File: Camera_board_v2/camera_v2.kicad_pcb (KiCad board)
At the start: 2 copper layers, 21.4 x 36.6 mm, 30 parts, among them J1 Conn_01x01, J2 Conn_01x05, J7 FC Connector, J8 I2C1 Breakout, Q1 BSS83P, Q2 BSS138, U2 TLV74315, U3 TLV74328, X1 CAMERA_OV2640

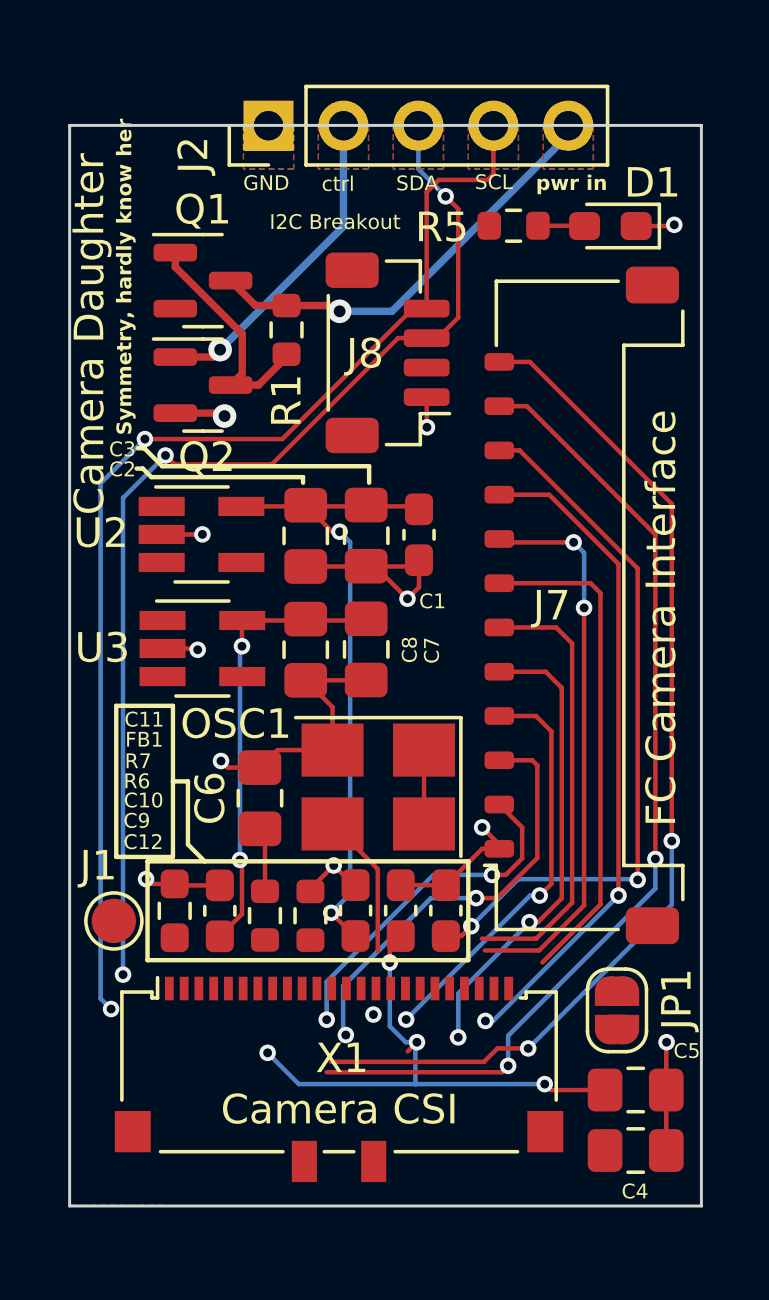
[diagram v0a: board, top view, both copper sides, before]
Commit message: finished?
everything is connected, but theres a few errors - idk how significant those are
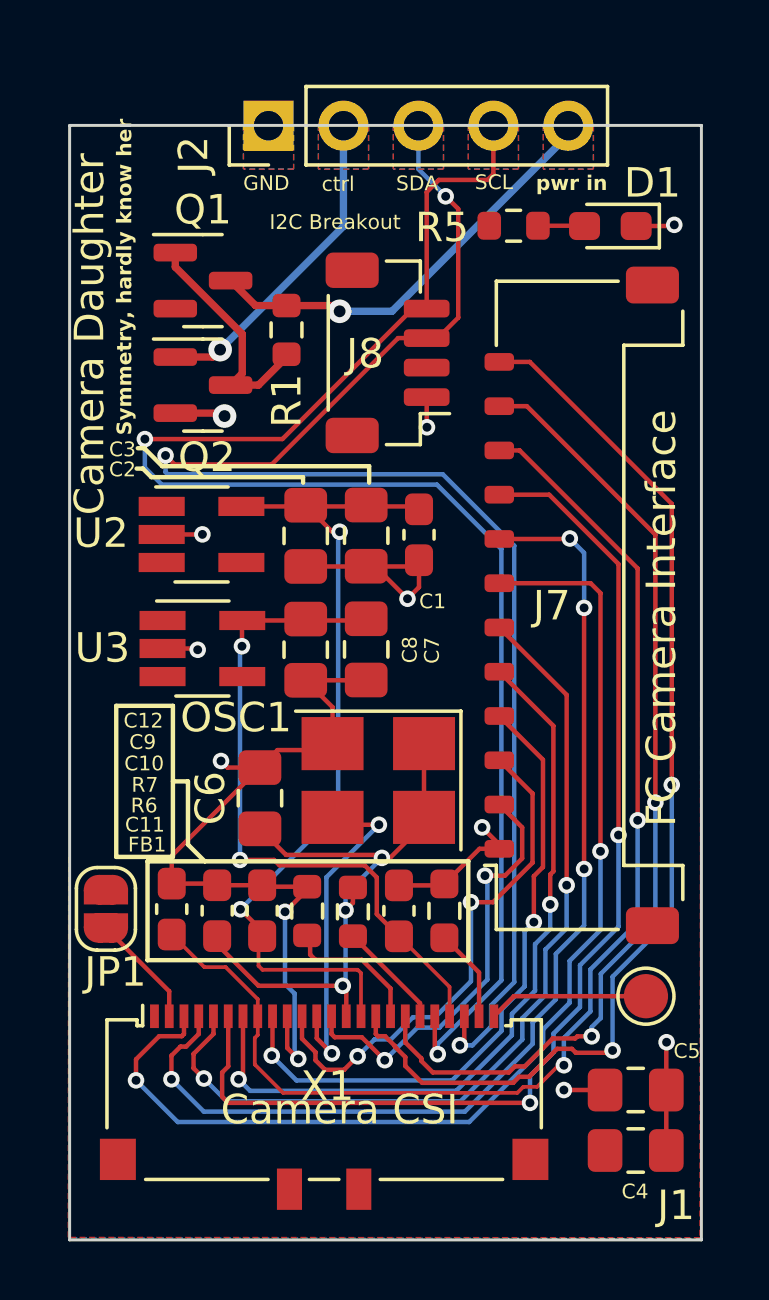
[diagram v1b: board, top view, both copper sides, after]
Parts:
- removed G***: LOGO, LOGO
- moved J1 18.2 mm to (166.5, 135.2)
- moved JP1 17.7 mm to (148.2, 132.2)
- moved C12 9.29 mm to (150.4, 132.2)
- moved FB1 9.14 mm to (159.7, 132.3)
- moved C9 6.22 mm to (151.9, 132.3)
- moved C11 6.07 mm to (158.1, 132.3)
- moved C10 3.17 mm to (153.5, 132.3)
- moved R6 2.98 mm to (156.6, 132.3)
- moved X1 1.07 mm to (155.6, 138.9)
- moved OSC1 0.22 mm to (157.4, 127.8)
- moved R7 0.19 mm to (155.0, 132.3)
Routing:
- net D4: track 16.9 -> 38.5 mm, vias 0 -> 2
- net ENAB_RF / D3: track 19.0 -> 36.7 mm, vias 2 -> 4
- net VBUS_RESET / PC: track 24.2 -> 41.6 mm
- net I2C_RESET / D2: track 22.5 -> 37.8 mm
- net D5: track 15.0 -> 30.0 mm, vias 0 -> 2
- net SDA1: track 37.2 -> 51.4 mm
- net SCL1: track 39.4 -> 52.8 mm
- net GND: track 36.1 -> 49.3 mm
- net D6: track 16.0 -> 26.1 mm
- net ENABLE_BURN / D7: track 14.0 -> 22.0 mm
- net 2.8V: track 15.6 -> 23.3 mm
- net 1.5V: track 22.2 -> 29.1 mm, vias 3 -> 2
- net Net-(OSC1-OUT): track 4.95 -> 11.6 mm, vias 0 -> 2
- net Net-(J1-Pin_1): track 0.00 -> 5.44 mm
- net Net-(X1-PWDN): track 0.24 -> 4.83 mm
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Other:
- board size 21.4 x 36.6 mm -> 21.4 x 37.8 mm

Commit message: might be too big
added meme to the back - board might be too long
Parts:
- added G***: LOGO, LOGO, B.Cu at (156.6, 121.0)
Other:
- board text added: "What do you mean I have to flip the whole board?"

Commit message: small fixes
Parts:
- moved JP1 0.25 mm to (148.4, 132.3)
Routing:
- net +3V3: track 22.6 -> 33.6 mm, vias 4 -> 6

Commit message: Updated Camera Board V2 with Production Files
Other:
- board text added: "Camera Daughter Board V2 By Nicole Maggard Updated By Kelly Williams C.2024"
- board text removed: "Camera Daughter Board V1 By Nicole Maggard"
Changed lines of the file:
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@@
 			)
 		)
-		(property "Footprint" ""
+		(property "Footprint" "Capacitor_SMD:C_0805_2012Metric_Pad1.18x1.45mm_HandSolder"
 			(at 0 0 -90)
 			(unlocked yes)
@@
 			)
 		)
-		(property "Footprint" ""
+		(property "Footprint" "Oscillator:Oscillator_SMD_SeikoEpson_SG8002CE-4Pin_3.2x2.5mm_HandSoldering"
 			(at 0 0 180)
 			(unlocked yes)
@@
 			)
 		)
-		(property "Footprint" ""
+		(property "Footprint" "Jumper:SolderJumper-2_P1.3mm_Open_RoundedPad1.0x1.5mm"
 			(at 0 0 90)
 			(unlocked yes)
@@
 			)
 		)
-		(property "Footprint" ""
+		(property "Footprint" "Capacitor_SMD:C_0603_1608Metric_Pad1.08x0.95mm_HandSolder"
 			(at 0 0 -90)
 			(unlocked yes)
@@
 			)
 		)
-		(property "Footprint" ""
+		(property "Footprint" "Capacitor_SMD:C_0805_2012Metric_Pad1.18x1.45mm_HandSolder"
 			(at 0 0 90)
 			(unlocked yes)
@@
 			)
 		)
-		(property "Footprint" ""
+		(property "Footprint" "Capacitor_SMD:C_0603_1608Metric_Pad1.08x0.95mm_HandSolder"
 			(at 0 0 90)
 			(unlocked yes)
@@
 			)
 		)
-		(property "Footprint" ""
+		(property "Footprint" "Capacitor_SMD:C_0805_2012Metric_Pad1.18x1.45mm_HandSolder"
 			(at 0 0 0)
 			(unlocked yes)
@@
 			)
 		)
-		(property "Footprint" ""
+		(property "Footprint" "Connector_Molex:Molex_Pico-Lock_504050-1291_1x12-1MP_P1.50mm_Horizontal"
 			(at 0 0 90)
 			(unlocked yes)
@@
 			)
 		)
-		(property "Footprint" ""
+		(property "Footprint" "Resistor_SMD:R_0603_1608Metric"
 			(at 0 0 90)
 			(unlocked yes)
@@
 			)
 		)
-		(property "Footprint" ""
+		(property "Footprint" "Package_TO_SOT_SMD:SOT-23-5_HandSoldering"
 			(at 0 0 0)
 			(unlocked yes)
@@
 			)
 		)
-		(property "Footprint" ""
+		(property "Footprint" "Capacitor_SMD:C_0603_1608Metric_Pad1.08x0.95mm_HandSolder"
 			(at 0 0 90)
 			(unlocked yes)
@@
 			)
 		)
-		(property "Footprint" ""
+		(property "Footprint" "Package_TO_SOT_SMD:SOT-23-5_HandSoldering"
 			(at 0 0 0)
 			(unlocked yes)
@@
 			)
 		)
-		(property "Footprint" ""
+		(property "Footprint" "Resistor_SMD:R_0603_1608Metric_Pad0.98x0.95mm_HandSolder"
 			(at 0 0 -90)
 			(unlocked yes)
@@
 			)
 		)
-		(property "Footprint" ""
+		(property "Footprint" "Capacitor_SMD:C_0603_1608Metric_Pad1.08x0.95mm_HandSolder"
 			(at 0 0 90)
 			(unlocked yes)
@@
 			)
 		)
-		(property "Footprint" ""
+		(property "Footprint" "Capacitor_SMD:C_0805_2012Metric_Pad1.18x1.45mm_HandSolder"
 			(at 0 0 -90)
 			(unlocked yes)
@@
 			)
 		)
-		(property "Footprint" ""
+		(property "Footprint" "Capacitor_SMD:C_0805_2012Metric_Pad1.18x1.45mm_HandSolder"
 			(at 0 0 -90)
 			(unlocked yes)
@@
 			)
 		)
-		(property "Footprint" ""
+		(property "Footprint" "TestPoint:TestPoint_Pad_D1.5mm"
 			(at 0 0 0)
 			(unlocked yes)
@@
 			)
 		)
-		(property "Footprint" ""
+		(property "Footprint" "Resistor_SMD:R_0603_1608Metric"
 			(at 0 0 -90)
 			(unlocked yes)
@@
 			)
 		)
-		(property "Footprint" ""
+		(property "Footprint" "Connector_PinHeader_2.54mm:PinHeader_1x05_P2.54mm_Vertical"
 			(at 0 0 90)
 			(unlocked yes)
@@
 			)
 		)
-		(property "Footprint" ""
+		(property "Footprint" "Capacitor_SMD:C_0603_1608Metric_Pad1.08x0.95mm_HandSolder"
 			(at 0 0 90)
 			(unlocked yes)
@@
 			)
 		)
-		(property "Footprint" ""
+		(property "Footprint" "LED_SMD:LED_0603_1608Metric_Pad1.05x0.95mm_HandSolder"
 			(at 0 0 180)
 			(unlocked yes)
@@
 			)
 		)
-		(property "Footprint" ""
+		(property "Footprint" "Connector_FFC-FPC:Molex_502244-2430_1x24-1MP_P0.5mm_Horizontal"
 			(at 0 0 0)
 			(unlocked yes)
@@
 			)
 		)
-		(property "Footprint" ""
+		(property "Footprint" "Capacitor_SMD:C_0805_2012Metric_Pad1.18x1.45mm_HandSolder"
 			(at 0 0 -90)
 			(unlocked yes)
@@
 			)
 		)
-		(property "Footprint" ""
+		(property "Footprint" "Package_TO_SOT_SMD:SOT-23"
 			(at 0 0 0)
 			(unlocked yes)
@@
 			)
 		)
-		(property "Footprint" ""
+		(property "Footprint" "Package_TO_SOT_SMD:SOT-23"
 			(at 0 0 0)
 			(unlocked yes)
@@
 			)
 		)
-		(property "Footprint" ""
+		(property "Footprint" "Connector_JST:JST_SH_BM04B-SRSS-TB_1x04-1MP_P1.00mm_Vertical"
 			(at 0 0 90)
 			(unlocked yes)
@@
 			)
 		)
-		(property "Footprint" ""
+		(property "Footprint" "Resistor_SMD:R_0603_1608Metric"
 			(at 0 0 0)
 			(unlocked yes)
@@
 			)
 		)
-		(property "Footprint" ""
+		(property "Footprint" "Resistor_SMD:R_0603_1608Metric"
 			(at 0 0 -90)
 			(unlocked yes)
@@
 			)
 		)
-		(property "Footprint" ""
+		(property "Footprint" "Capacitor_SMD:C_0805_2012Metric_Pad1.18x1.45mm_HandSolder"
 			(at 0 0 0)
 			(unlocked yes)
@@
 			)
 		)
-		(property "Footprint" ""
+		(property "Footprint" "LOGO"
 			(at 0 0 180)
 			(unlocked yes)
@@
 	)
 	(gr_text "What do you mean I have\nto flip the whole board?"
-		(at 167.8 113.6 0)
+		(at 167.8 120 0)
 		(layer "B.SilkS")
 		(effects
@@
 		)
 	)
-	(gr_text "Camera Daughter Board V1\nBy Nicole Maggard"
-		(at 157.65 111.3 0)
+	(gr_text "Camera Daughter Board V2\nBy Nicole Maggard\nUpdated By Kelly Williams\nC.2024"
+		(at 157.8 114.5 0)
 		(layer "B.SilkS")
 		(effects
